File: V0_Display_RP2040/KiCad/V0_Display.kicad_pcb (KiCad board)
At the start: 4 copper layers, 80 x 35 mm, 46 parts, among them J2 I2C Header 1, J3 SWD, J4 USB-TYPE-C-018, J7 USB_Header, J8 Conn_01x02, SW1 MJTP1230A, SW5 MJTP1230A, SW6 MJTP1230A, SW7 EN11-HSB1AF15, U1 AP2127K-3.3, U2 USBLC6-2P6, U3 74LVC1G17, U4 W25Q16JVUXIQ_TR, U5 RP2040, Y1 12Mhz

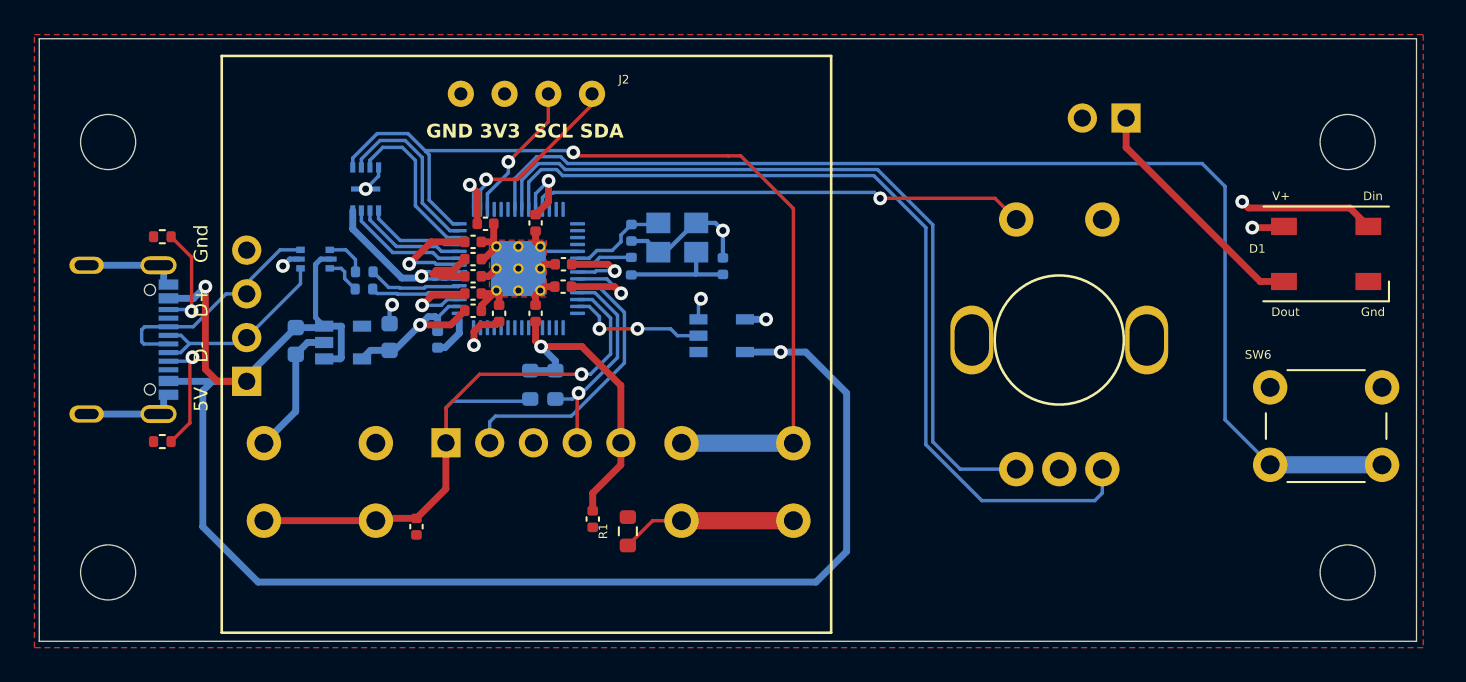
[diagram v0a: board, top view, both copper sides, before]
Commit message: Several updates
Update to 2 layer board
vertical USB connector
updated fonts
Regenerated gerbers, BOM, and placement file
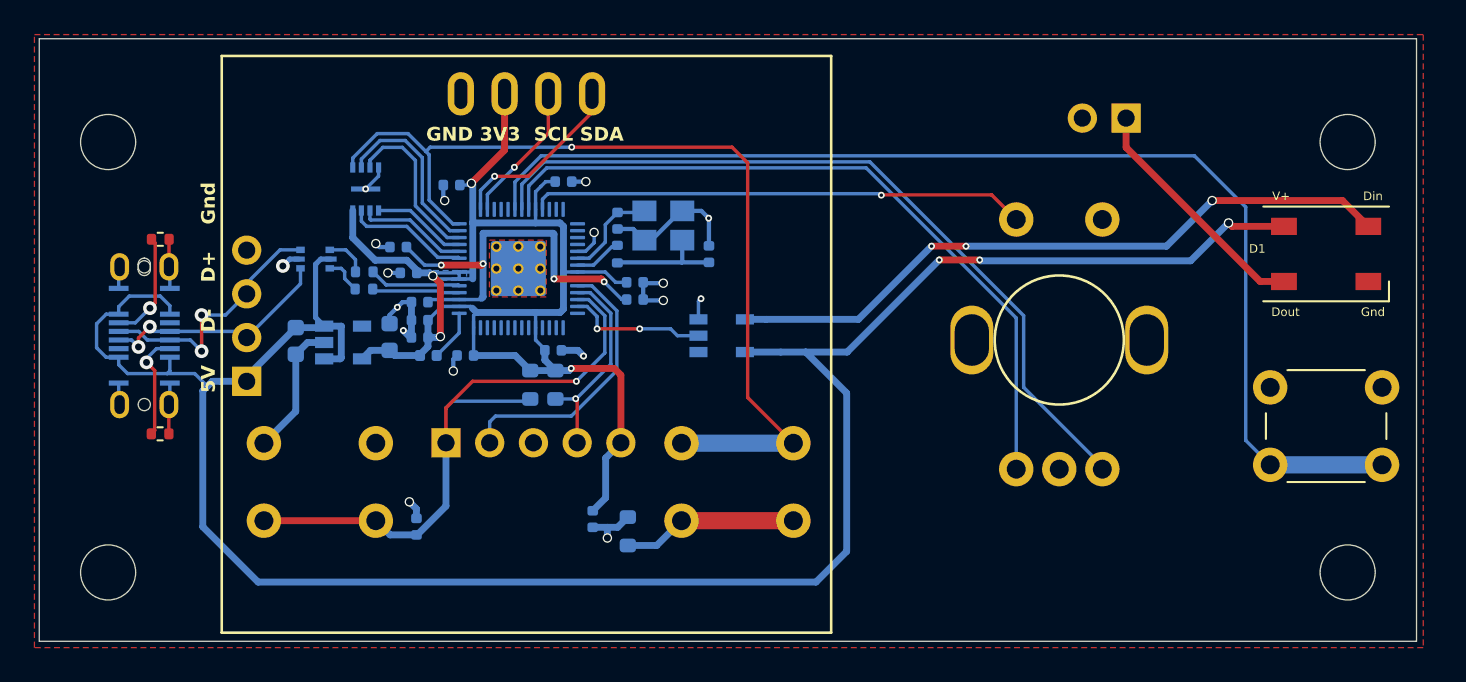
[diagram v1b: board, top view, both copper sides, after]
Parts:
- removed J4: USB-TYPE-C-018, Voron0 2040 library:GCT_USB4105-GF-A
- added J1: USB4145-03-0230-C_REVA2, USB4145-03-0230-C_REVA2:GCT_USB4145-03-0230-C_REVA2, B.Cu at (91.3, 66.9)
- C1, C2: footprint Voron0 2040 library:C_0603_1608Metric -> Voron0 2040 display:C_0603_1608Metric
- C10: value 0.1uf -> 1uf; footprint Voron0 2040 library:C_0402_1005Metric -> Voron0 2040 display:C_0402_1005Metric; moved to B.Cu
- C11, C12, C13, C14, C15, C16, C17, C5, C6, C7, C8, C9: footprint Voron0 2040 library:C_0402_1005Metric -> Voron0 2040 display:C_0402_1005Metric; moved to B.Cu
- C3, C4: value 27pf -> 30pf; footprint Voron0 2040 library:C_0402_1005Metric -> Voron0 2040 display:C_0402_1005Metric
- D1: footprint Voron0 2040 library:LED_WS2812B_PLCC4_5.0x5.0mm_P3.2mm -> Voron0 2040 display:LED_WS2812B_PLCC4_5.0x5.0mm_P3.2mm
- H1, H2, H3, H4: footprint Voron0 2040 library:MountingHole_3.2mm_M3 -> Voron0 2040 display:MountingHole_3.2mm_M3
- J2: footprint Voron0 2040 library:1pt3in_OLED -> Voron0 2040 display:1pt3in_OLED
- J3: footprint Voron0 2040 library:PinHeader_1x05_P2.54mm_Vertical -> Voron0 2040 display:PinHeader_1x05_P2.54mm_Vertical
- J7: footprint Voron0 2040 library:PinHeader_1x04_P2.54mm_Vertical -> Voron0 2040 display:PinHeader_1x04_P2.54mm_Vertical
- J8: footprint Voron0 2040 library:PinHeader_1x02_P2.54mm_Vertical -> Voron0 2040 display:PinHeader_1x02_P2.54mm_Vertical
- L1: footprint Voron0 2040 library:L_0402_1005Metric -> Voron0 2040 display:L_0402_1005Metric
- R1: footprint Voron0 2040 library:R_0603_1608Metric -> Voron0 2040 display:R_0603_1608Metric; moved to B.Cu
- R2, R5, R6, R7, R8: footprint Voron0 2040 library:R_0402_1005Metric -> Voron0 2040 display:R_0402_1005Metric
- R3, R4: footprint Voron0 2040 library:R_0603_1608Metric -> Voron0 2040 display:R_0603_1608Metric
- SW1: value MJTP1230A -> RESET; footprint Voron0 2040 library:SW_PUSH_6mm -> Voron0 2040 display:SW_PUSH_6mm
- SW5: value MJTP1230A -> BOOTSEL; footprint Voron0 2040 library:SW_PUSH_6mm -> Voron0 2040 display:SW_PUSH_6mm
- SW6: value MJTP1230A -> Killswitch; footprint Voron0 2040 library:SW_PUSH_6mm -> Voron0 2040 display:SW_PUSH_6mm
- SW7: value EN11-HSB1AF15 -> Rotary_Encoder_Switch; footprint Voron0 2040 library:EN11_Encoder -> Voron0 2040 display:EN11_Encoder
- U1: footprint Voron0 2040 library:SOT-23-5 -> Voron0 2040 display:SOT-23-5
- U2: footprint Voron0 2040 library:SOT-666 -> Voron0 2040 display:SOT-666
- U3: footprint Voron0 2040 library:SOT-753 -> Voron0 2040 display:SOT-753
- U4: footprint Voron0 2040 library:IC_W25Q16JVUXIQ_TR -> Voron0 2040 display:IC_W25Q16JVUXIQ_TR
- U5: footprint Voron0 2040 library:RP2040-QFN-56 -> Voron0 2040 display:RP2040-QFN-56
- Y1: footprint Voron0 2040 library:Crystal_SMD_3225-4Pin_3.2x2.5mm -> Voron0 2040 display:Crystal_SMD_3225-4Pin_3.2x2.5mm
- moved C10 6.87 mm to (107.3, 67.0), turned to 180 degrees
- moved C17 5.30 mm to (106.6, 63.2), turned to 180 degrees
- moved C7 5.12 mm to (106.0, 61.8), turned to 180 degrees
- moved C9 4.68 mm to (107.3, 65.0), turned to 180 degrees
- moved C14 4.62 mm to (109.9, 68.0), turned to 180 degrees
- moved C12 4.48 mm to (109.1, 58.1), turned to 180 degrees
- moved C11 4.28 mm to (119.8, 63.8), turned to 0 degrees
- moved C6 4.24 mm to (119.8, 64.8), turned to 0 degrees
- moved C15 3.81 mm to (115.0, 67.8), turned to 0 degrees
- moved C16 3.15 mm to (107.3, 66.0), turned to 180 degrees
- moved C13 2.90 mm to (115.6, 58.0), turned to 0 degrees
- moved L1 1.08 mm to (107.8, 68.0), turned to 0 degrees
- moved C4 1.07 mm to (124.1, 62.2)
- moved R2 1.07 mm to (118.8, 62.2)
- moved Y1 1.07 mm to (121.4, 60.5)
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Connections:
- U5 pad 8: Encoder_A -> Encoder_B
- U5 pad 9: Encoder_B -> Encoder_A
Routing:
- net 3.3V: track 62.2 -> 84.9 mm, vias 7 -> 4
- net 1.1V: track 17.7 -> 26.1 mm, vias 3 -> 4
- net Encoder_B: track 52.1 -> 45.7 mm
- net Encoder_A: track 45.6 -> 42.5 mm
- net D-: track 12.2 -> 14.1 mm, vias 0 -> 2
- net D+: track 13.5 -> 15.1 mm, vias 0 -> 2
- net Net-(D1-DIN): track 40.8 -> 39.7 mm, vias 2 -> 3
- net Net-(J1-CC1): track 7.18 -> 6.24 mm
- net SWDIO: track 12.9 -> 12.0 mm
- net VBUS: track 128.6 -> 127.8 mm
- net RUN: track 38.5 -> 39.1 mm
- net GND: track 48.6 -> 48.0 mm, vias 5 -> 17
- net SWDCLK: track 16.8 -> 16.2 mm
- net OSC_OUT: track 3.31 -> 2.79 mm
- removed copper zone on In1.Cu, net 1.1V
- removed copper zone on In2.Cu, net 3.3V
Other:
- copper layers 4 -> 2
- board text added: "V0-2040 Display V1"
- board text added: "[t]"
- board text removed: "[t] V0-2040 Display V1.2"

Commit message: Update #2
Changed to SMD push buttons
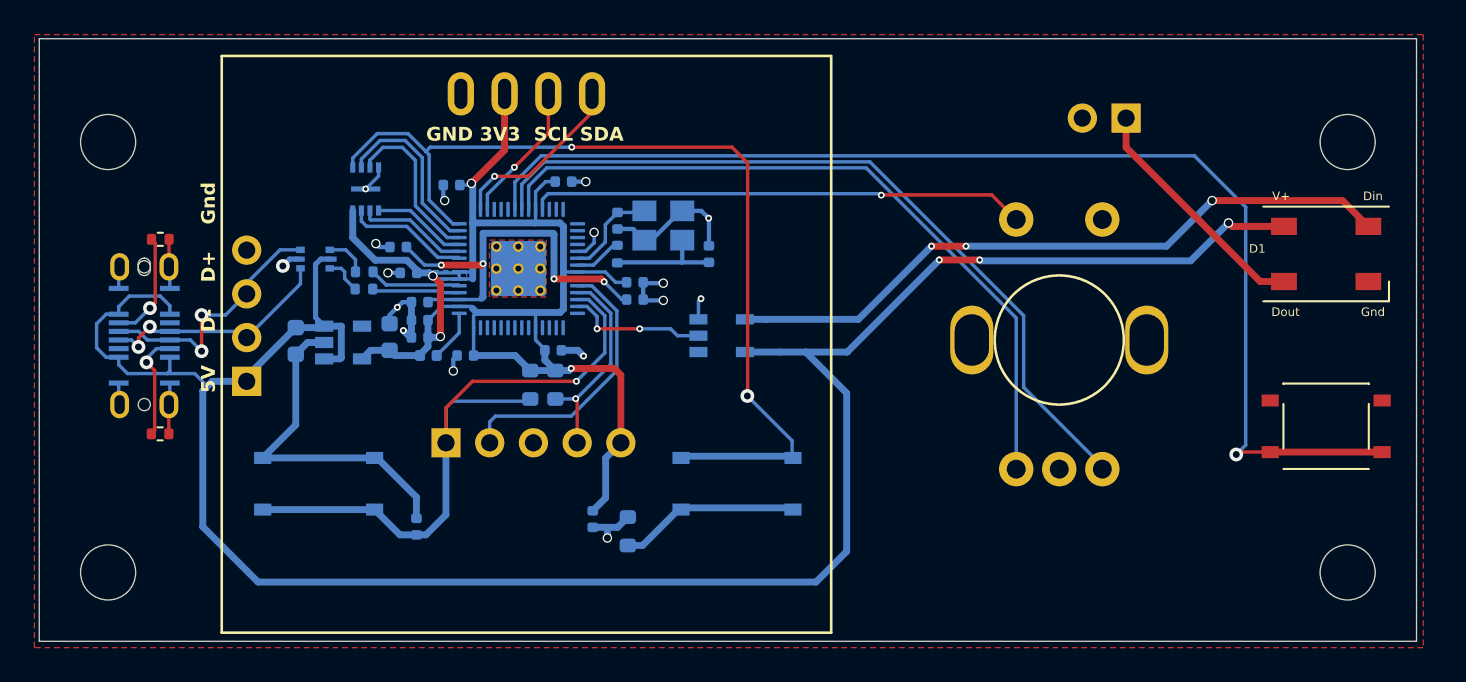
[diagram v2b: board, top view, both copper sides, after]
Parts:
- SW1, SW5, SW6: footprint Voron0 2040 display:SW_PUSH_6mm -> Library:SW_Push_1P1T_NO_4.5x4.5mm
- moved SW1 4.07 mm to (101.4, 75.5)
- moved SW5 4.03 mm to (125.7, 75.5)
- moved SW6 3.96 mm to (159.9, 72.2)
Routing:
- net GND: track 48.0 -> 58.9 mm, vias 17 -> 16
- net Kill_Switch: track 68.0 -> 69.0 mm, vias 0 -> 1
- net QSPI_SS: track 54.1 -> 54.9 mm, vias 1 -> 2
- net RUN: track 39.1 -> 39.8 mm

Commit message: Update V0_Display.kicad_pcb
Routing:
- net GND: vias 16 -> 17

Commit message: Usability updates to hardware
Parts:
- removed J1: USB4145-03-0230-C_REVA2, USB4145-03-0230-C_REVA2:GCT_USB4145-03-0230-C_REVA2
- removed R5, R6: 5.1K, Voron0 2040 display:R_0402_1005Metric
- added H5: MountingHole, Library:VoronLogo_6pt5mm_silkScreen, B.Cu at (131.0, 59.5)
- added J4: USB_B_Micro, Library:MolexVertical&Horizontal_MicroB, B.Cu at (87.9, 67.2)
- added J5: GPIO, Connector_PinHeader_2.54mm:PinHeader_1x03_P2.54mm_Vertical, B.Cu at (104.2, 68.7)
- added R9: 10k, Voron0 2040 display:R_0603_1608Metric, B.Cu at (106.0, 52.2)
- J2: footprint Voron0 2040 display:1pt3in_OLED -> Library:1pt3in_OLED
- moved R1 27.9 mm to (106.0, 53.8), turned to 180 degrees
- moved C1 20.6 mm to (115.9, 80.4), turned to 90 degrees
- moved U1 14.6 mm to (112.8, 78.0), turned to 90 degrees
- moved C12 7.07 mm to (102.1, 58.8), turned to 90 degrees
- moved C2 6.58 mm to (111.8, 69.1), turned to -90 degrees
- moved C15 4.57 mm to (110.5, 68.5), turned to -90 degrees
- moved J7 3.19 mm to (94.7, 71.5)
- moved U2 1.26 mm to (100.9, 63.7)
- moved C14 0.64 mm to (109.5, 68.5), turned to -90 degrees
- moved C7 0.24 mm to (105.9, 61.5)
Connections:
- R1 pad 1: Net-(SW5-B) -> Net-(SW5-A)
- R1 pad 2: GND -> QSPI_SS
- SW5 pad 1: QSPI_SS -> Net-(SW5-A)
- SW5 pad 2: Net-(SW5-B) -> GND
- U5 pad 31: unconnected-(U5-GPIO20-Pad31) -> GPIO20
- U5 pad 32: unconnected-(U5-GPIO21-Pad32) -> GPIO21
- U5 pad 34: unconnected-(U5-GPIO22-Pad34) -> GPIO22
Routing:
- net Net-(SW5-A): track 0.00 -> 42.5 mm, vias 0 -> 2
- net QSPI_SS: track 54.9 -> 14.1 mm, vias 2 -> 0
- net GND: track 58.9 -> 93.4 mm, vias 17 -> 11
- net GPIO22: track 0.00 -> 16.1 mm, vias 0 -> 1
- net GPIO21: track 0.00 -> 14.5 mm, vias 0 -> 1
- net GPIO20: track 0.00 -> 11.5 mm, vias 0 -> 1
- net VBUS: track 127.8 -> 116.4 mm
- net Net-(SW5-B): track 10.4 -> 0.00 mm
- net Net-(J1-CC2): track 6.38 -> 0.00 mm, vias 1 -> 0
- net Net-(J1-CC1): track 6.24 -> 0.00 mm, vias 1 -> 0
- net 3.3V: track 84.9 -> 88.0 mm, vias 4 -> 5
- net SDA: track 10.5 -> 9.46 mm
- net Encoder_Switch: track 28.9 -> 29.8 mm
- net OUT_D+: track 2.44 -> 1.70 mm
- net D+: track 15.1 -> 14.4 mm, vias 2 -> 0
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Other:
- board text added: "20 21 22"
- board text added: "KILLSWITCH"
